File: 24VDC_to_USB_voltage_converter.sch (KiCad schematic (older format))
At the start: 29 parts, among them J1 Conn_01x02, J2 USB_A, J3 Conn_01x02, Q1 CPH6341-TL-W, U1 TPS54308

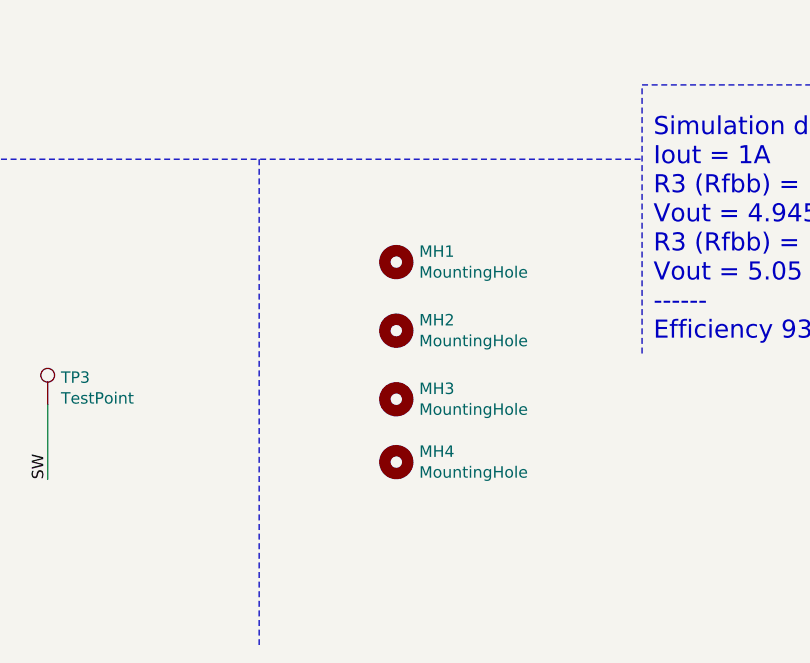
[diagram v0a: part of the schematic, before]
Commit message: Adding final changes and exporting Gerbers
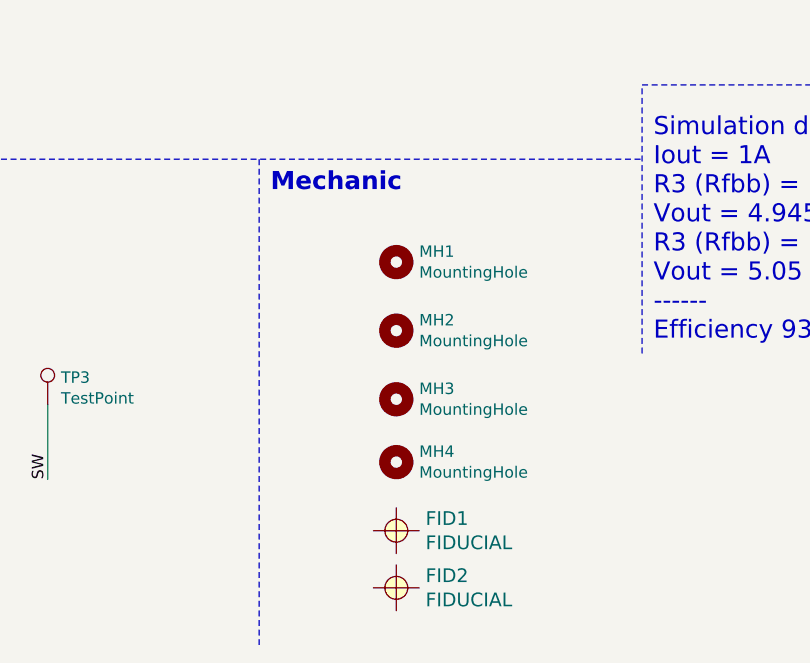
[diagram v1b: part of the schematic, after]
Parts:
- added FID1, FID2: FIDUCIAL, Fiducial:Fiducial_0.75mm_Dia_1.5mm_Outer, symbol Local-special:FIDUCIAL
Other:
- note added: "Mechanic"
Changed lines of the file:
@@
 EESchema Schematic File Version 4
+LIBS:24VDC_to_USB_voltage_converter-cache
 EELAYER 26 0
 EELAYER END
@@
 Text Label 9350 3550 0    50   ~ 0
 SHIELD
+Text Notes 5350 5825 0    79   ~ 16
+Mechanic
+$Comp
+L Local-special:FIDUCIAL FID1
+U 1 1 5C784501
+P 5900 7300
+F 0 "FID1" H 6028 7353 60  0000 L CNN
+F 1 "FIDUCIAL" H 6028 7247 60  0000 L CNN
+F 2 "Fiducial:Fiducial_0.75mm_Dia_1.5mm_Outer" H 6028 7194 60  0001 L CNN
+F 3 "" H 5900 7300 60  0000 C CNN
+	1    5900 7300
+	1    0    0    -1
+$EndComp
+$Comp
+L Local-special:FIDUCIAL FID2
+U 1 1 5C784735
+P 5900 7550
+F 0 "FID2" H 6028 7603 60  0000 L CNN
+F 1 "FIDUCIAL" H 6028 7497 60  0000 L CNN
+F 2 "Fiducial:Fiducial_0.75mm_Dia_1.5mm_Outer" H 6028 7444 60  0001 L CNN
+F 3 "" H 5900 7550 60  0000 C CNN
+	1    5900 7550
+	1    0    0    -1
+$EndComp
 $EndSCHEMATC

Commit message: Finishing the board and creating gerbers for ordering
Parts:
- FID1, FID2: footprint Fiducial:Fiducial_0.75mm_Dia_1.5mm_Outer -> footprints:FIDUCIAL
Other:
- note added: "veći fiduciali"
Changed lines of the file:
@@
 F 0 "FID1" H 6028 7353 60  0000 L CNN
 F 1 "FIDUCIAL" H 6028 7247 60  0000 L CNN
-F 2 "Fiducial:Fiducial_0.75mm_Dia_1.5mm_Outer" H 6028 7194 60  0001 L CNN
+F 2 "footprints:FIDUCIAL" H 6028 7194 60  0001 L CNN
 F 3 "" H 5900 7300 60  0000 C CNN
 	1    5900 7300
@@
 F 0 "FID2" H 6028 7603 60  0000 L CNN
 F 1 "FIDUCIAL" H 6028 7497 60  0000 L CNN
-F 2 "Fiducial:Fiducial_0.75mm_Dia_1.5mm_Outer" H 6028 7444 60  0001 L CNN
+F 2 "footprints:FIDUCIAL" H 6028 7444 60  0001 L CNN
 F 3 "" H 5900 7550 60  0000 C CNN
 	1    5900 7550
 	1    0    0    -1
 $EndComp
+Text Notes 5350 7250 0    118  ~ 24
+veći fiduciali
 $EndSCHEMATC

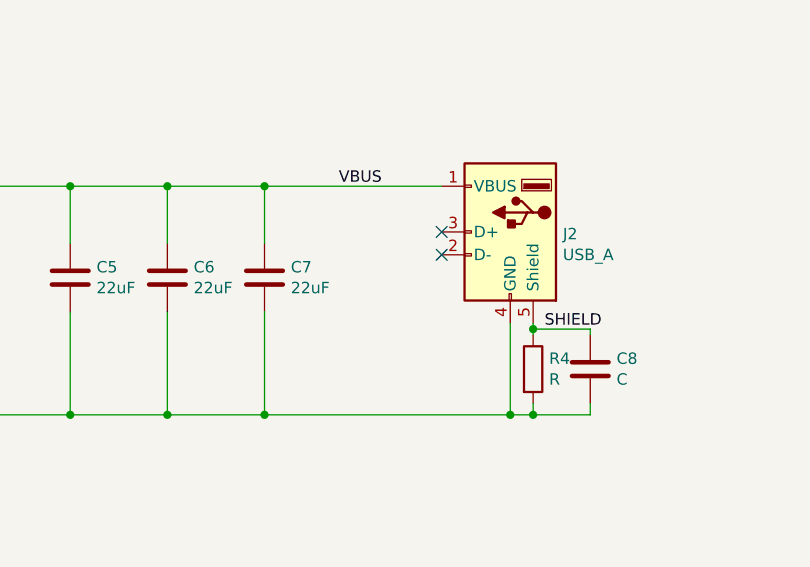
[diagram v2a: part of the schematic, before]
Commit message: Adding short resistor between d+ and d-, small changes in PCB
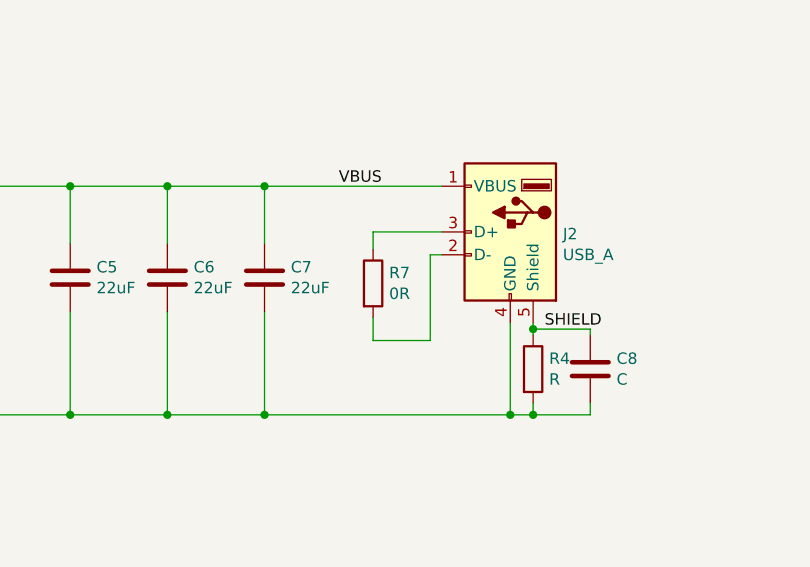
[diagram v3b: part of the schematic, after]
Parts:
- added R7: 0R, Resistor_SMD:R_0603_1608Metric, symbol Device:R
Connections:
- net at J2.2 (D-): now also R7.2
- net at J2.3 (D+): now also R7.1
- no-connect marks 2 -> 0
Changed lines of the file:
@@
 	6700 3125 6700 2925
 Connection ~ 6700 3125
-NoConn ~ 8900 3125
-NoConn ~ 8900 3225
 $Comp
 L Device:C C5
@@
 Connection ~ 8125 2925
 Wire Wire Line
-	8125 2925 8900 2925
-Wire Wire Line
 	6700 3925 7275 3925
 Wire Wire Line
@@
 Wire Wire Line
 	8125 3475 8125 3925
-Connection ~ 8125 3925
-Wire Wire Line
-	8125 3925 9200 3925
 $Comp
 L Device:R R4
@@
 Text Notes 5350 7250 0    118  ~ 24
 veći fiduciali
+Wire Wire Line
+	8125 2925 8900 2925
+Wire Wire Line
+	8125 3925 9200 3925
+Connection ~ 8125 3925
+$Comp
+L Device:R R7
+U 1 1 5C82DD6E
+P 8600 3350
+F 0 "R7" H 8670 3396 50  0000 L CNN
+F 1 "0R" H 8670 3305 50  0000 L CNN
+F 2 "Resistor_SMD:R_0603_1608Metric" V 8530 3350 50  0001 C CNN
+F 3 "~" H 8600 3350 50  0001 C CNN
+	1    8600 3350
+	1    0    0    -1
+$EndComp
+Wire Wire Line
+	8900 3125 8600 3125
+Wire Wire Line
+	8600 3125 8600 3200
+Wire Wire Line
+	8600 3500 8600 3600
+Wire Wire Line
+	8600 3600 8850 3600
+Wire Wire Line
+	8850 3600 8850 3225
+Wire Wire Line
+	8850 3225 8900 3225
 $EndSCHEMATC

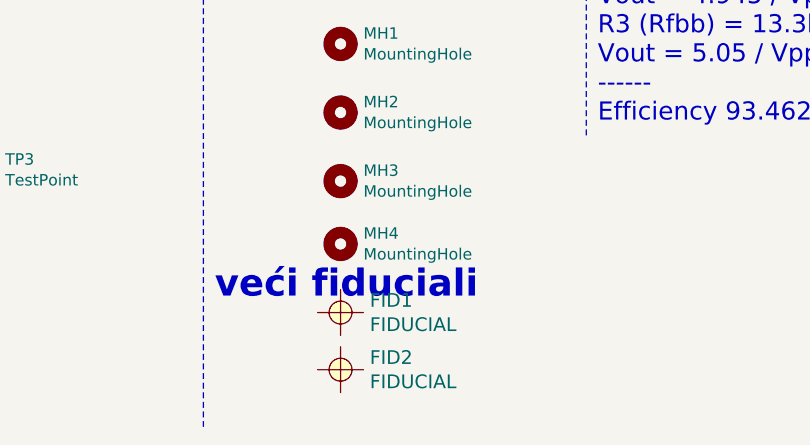
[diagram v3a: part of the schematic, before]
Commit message: Adding PDF file, removing comments from schematic, adding scope image in schematic
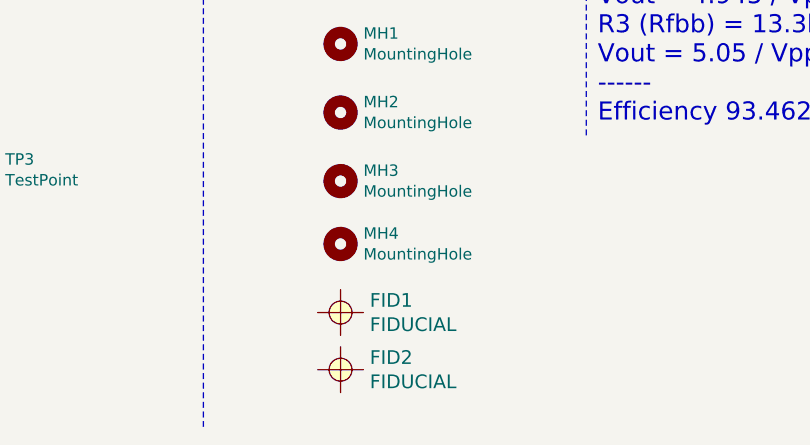
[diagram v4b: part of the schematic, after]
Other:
- note removed: "veći fiduciali"

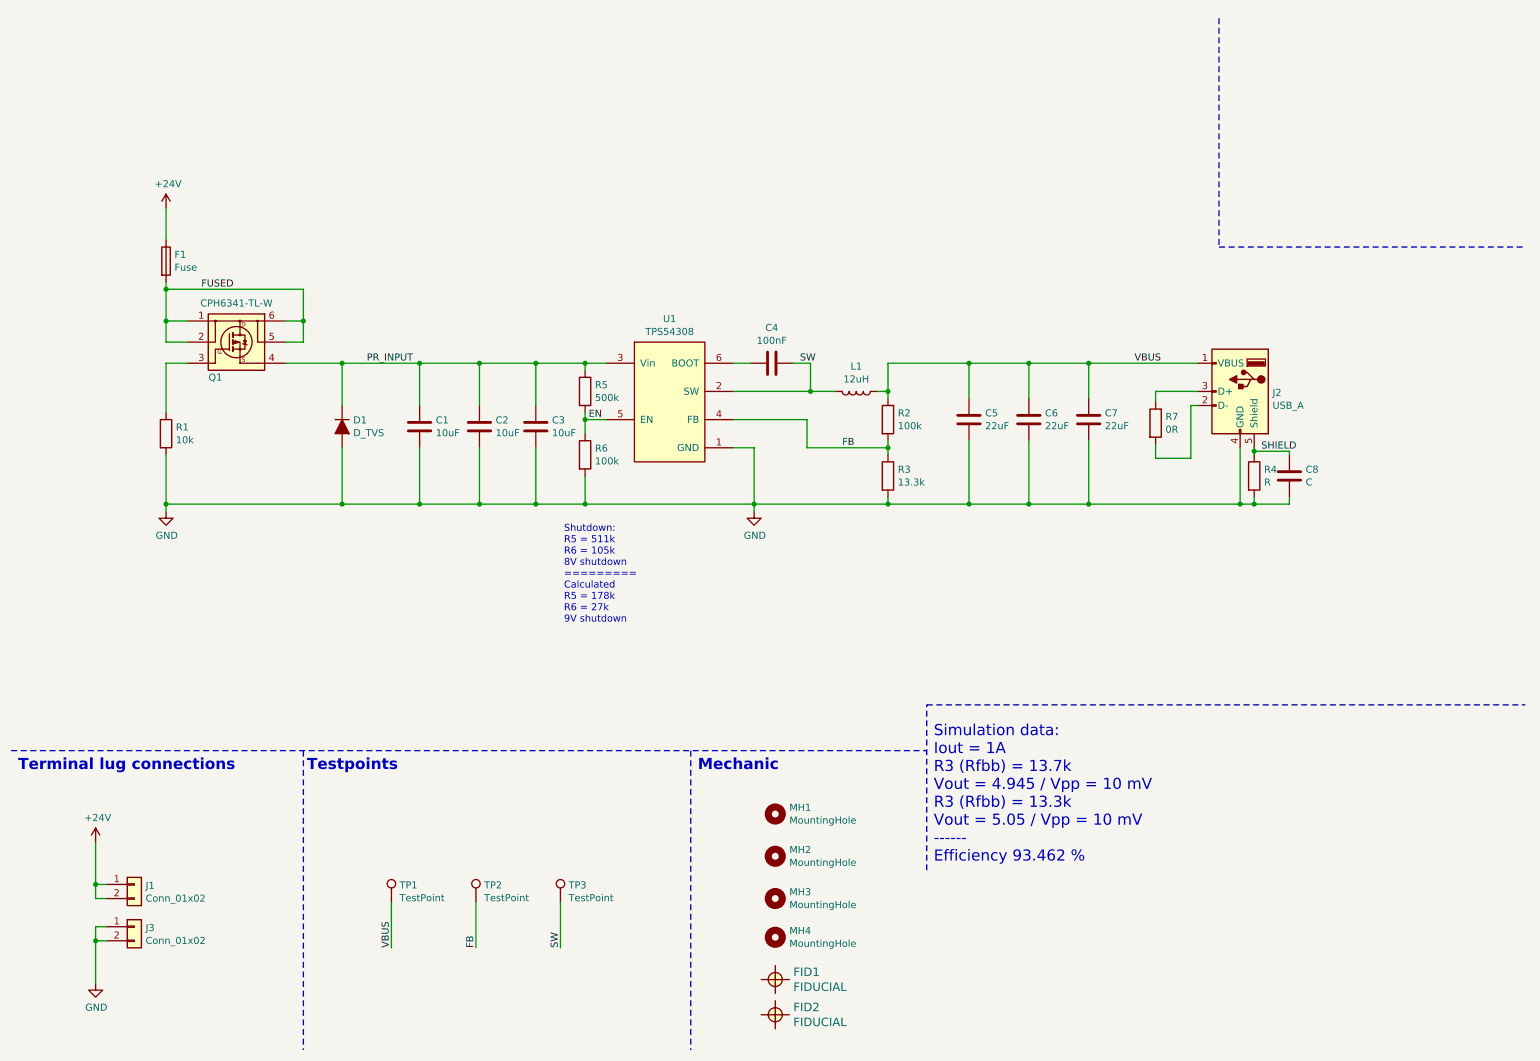
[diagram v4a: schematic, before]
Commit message: Adding noise characteristic to schematic and rearranging some items in schematic
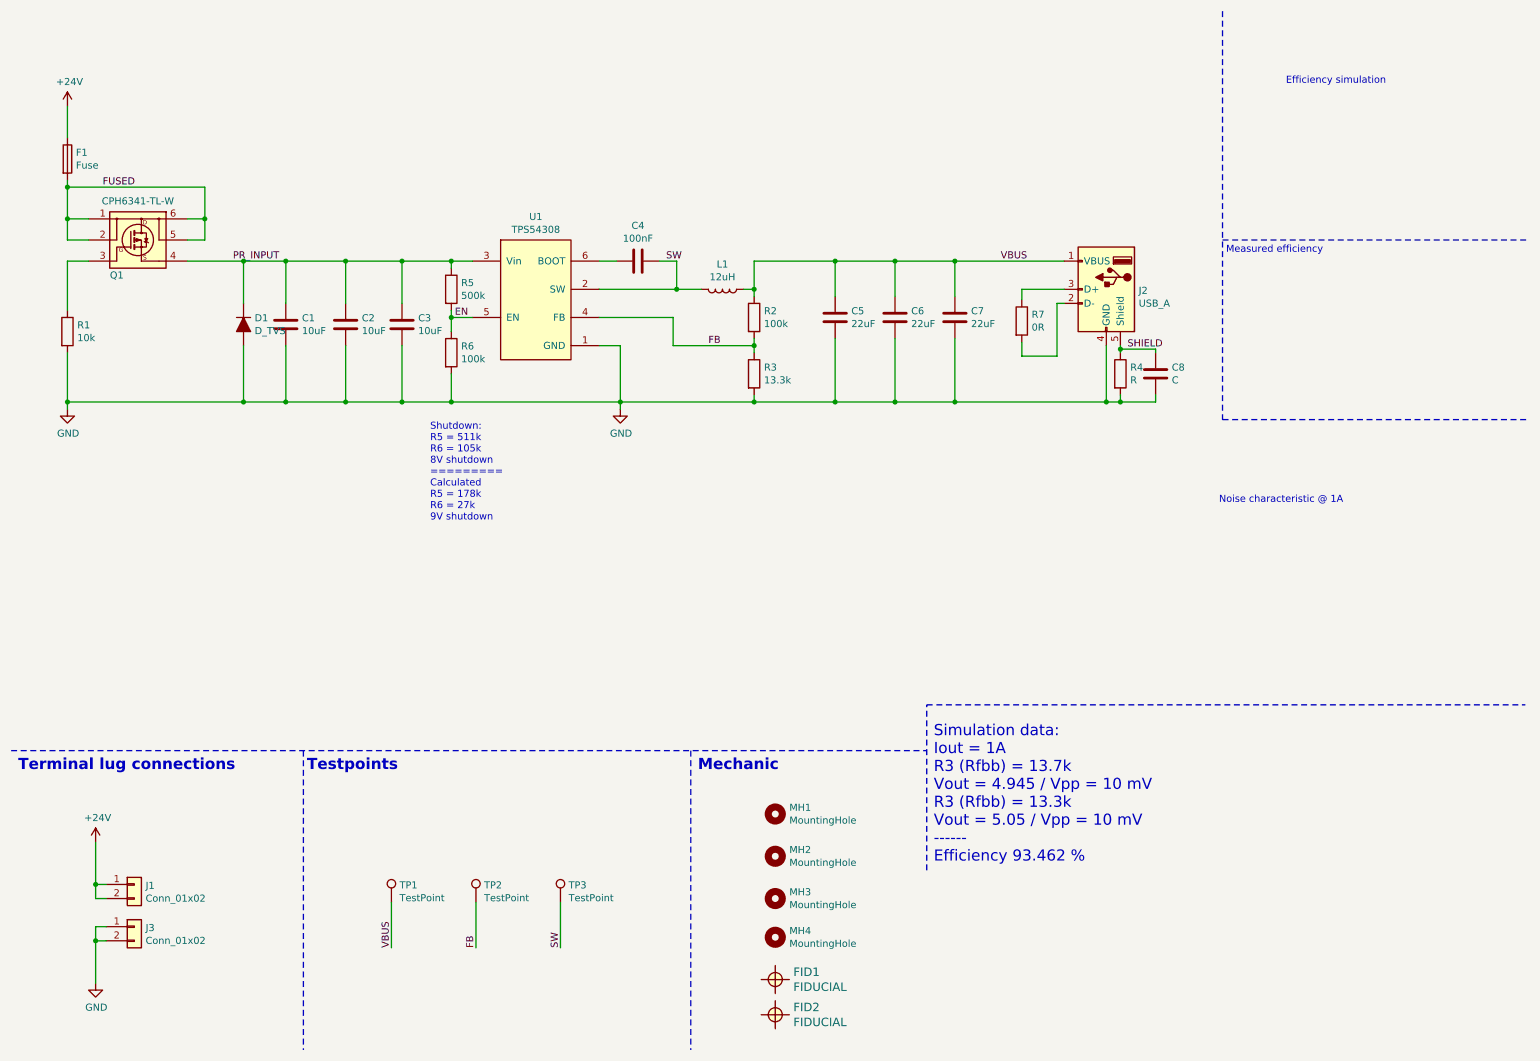
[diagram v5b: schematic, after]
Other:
- note added: "Efficiency simulation"
- note added: "Measured efficiency"
- note added: "Noise characteristic @ 1A"
- moved on the sheet: C1, C2, C3, C4, C5, C6, C7, C8, D1, F1, J2, L1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

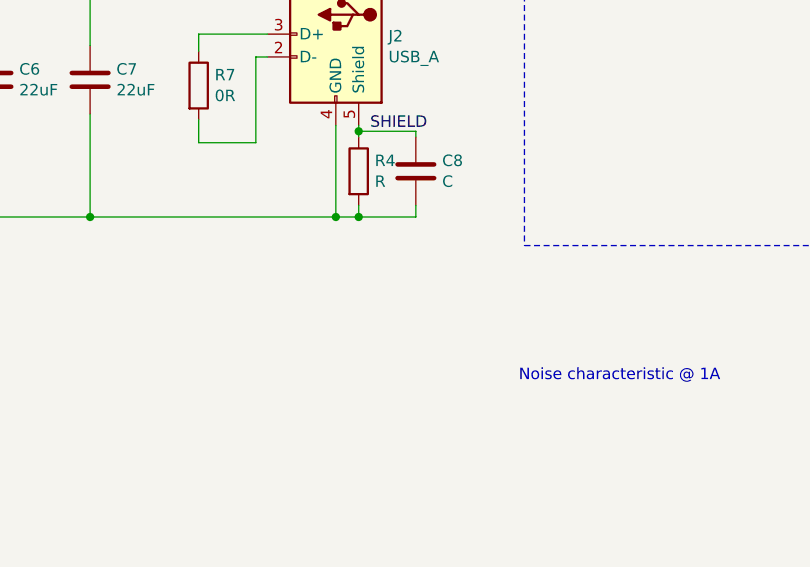
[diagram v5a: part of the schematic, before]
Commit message: Adding one comment to schematic
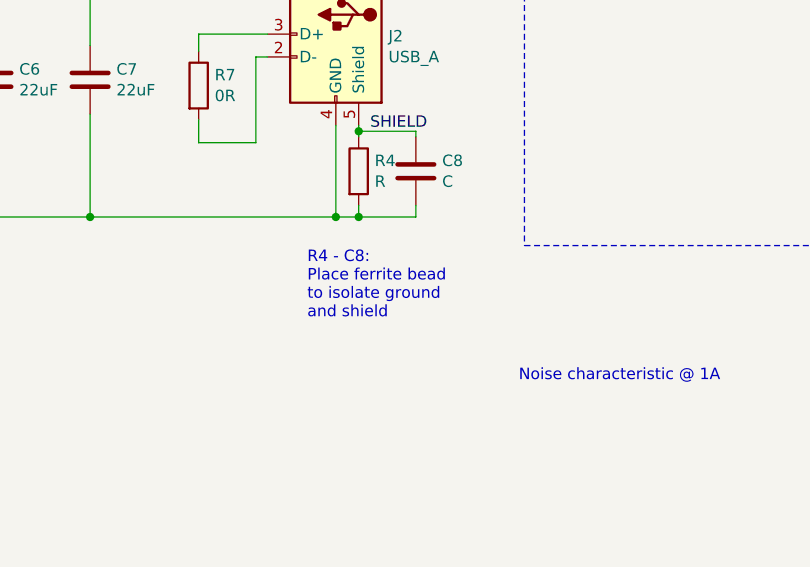
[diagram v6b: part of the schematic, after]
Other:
- note added: "R4 - C8:\nPlace ferrite bead \nto isolate ground\nand shield"
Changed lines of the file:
@@
 EESchema Schematic File Version 4
 LIBS:24VDC_to_USB_voltage_converter-cache
-EELAYER 26 0
+EELAYER 29 0
 EELAYER END
 $Descr A4 11693 8268
@@
 Wire Wire Line
 	875  3200 875  3250
+Text Notes 8125 3650 0    50   ~ 0
+R4 - C8:\nPlace ferrite bead \nto isolate ground\nand shield
 $EndSCHEMATC
